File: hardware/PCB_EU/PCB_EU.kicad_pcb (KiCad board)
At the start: 4 copper layers, 100 x 100 mm, 203 parts, among them J101 24 V IN, J201 UART 3V3, J301 MEM2061 SPI, J401 SHT 3V3 / GND, J402 SHT SDA / SCL, J403 FLOAT / GND, J411 FAN1: GND / +12, J412 FAN1: TACH / PWM, J421 FAN2: GND / +12, J422 FAN2: TACH / PWM, J501 LED1 + / GND, J601 LED2 + / GND, J602 BAR2 + / GND, J701 PTC + / RETURN, J702 PUMP + / RETURN, Q102 IRF1010ESPBF, Q411 FAN1 AO3422, Q421 FAN2 AO3422, Q501 TK22E10N1, Q601 TK22E10N1, Q701 BC847B-DIO, Q702 BC857B, Q703 IRF1010ESPBF, Q704 AO3422, SW201 RESET, SW202 BOOT, U101 L7987 3A, U102 INA226, U201 AP63203WU-7, U202 ESP32-WROOM-32E-N4, U301 MCP7940N-I/SN, U401 USBLC6-2SC6, U402 USBLC6-2SC6, U501 LM3429MH/NOPB, U601 LM3429MH/NOPB, U802 LM2903D-ST, Y301 32.768k CL7p

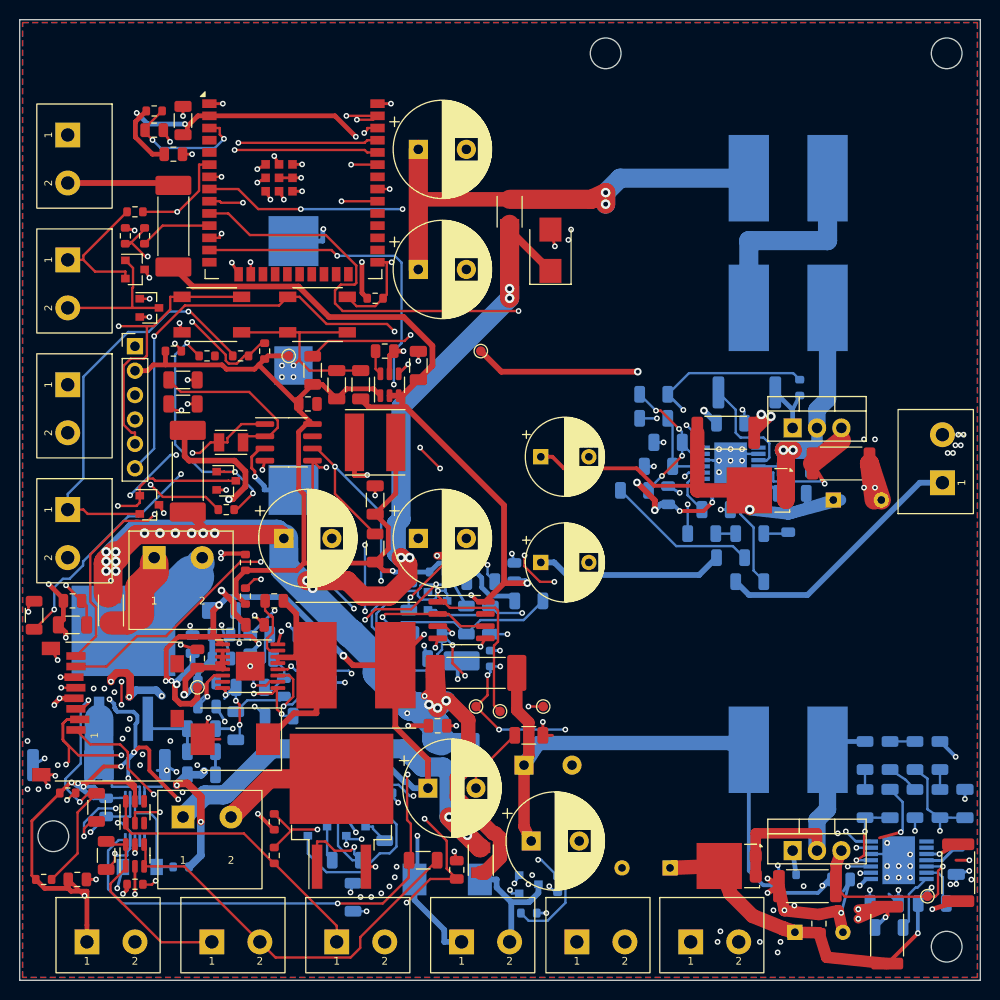
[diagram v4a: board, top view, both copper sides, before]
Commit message: PCB_EU: all terminals at the board edges, no HS2, fans on KF2510-4A, SHT4x on XH2.54-4P-90
Per Igors (22.10.2026):
- stack stated as 1 oz outer / 0.5 oz inner in DESIGN.md;
- heatsink HS2 removed from the LED2 channel (Q601 runs without a heatsink,
  about 54 C rise, to be measured on the prototype), freed area used for the
  pump terminal J702 and its parts at the right edge;
- J101, J201, J411, J421, J401, J403, J701, J702 moved so that every cable
  entry faces the board edge; J701 changed from DG301R to DG306;
- fan connectors J411/J421 are 4-pin KF2510-4A headers (Molex KK-254
  footprint), J412/J422 removed;
- SHT4x on one right-angle XH2.54-4P-90 header J401 (JST XH S4B-XH-A
  footprint), J402 removed;
- input, trunk and PTC copper re-routed in routing.json; the F101.2 trunk
  now starts with a 2.4 mm neck inside the pad (it was not attached before);
- BOM: quantities and total (82.50 EUR) unchanged, the new rows have no shop
  or price and are flagged for the BOM review.

Checks (KiCad 10.0.7): ERC 0, 56 connectivity checks, 22639 placement checks,
DRC 0 / parity 0 / unconnected 0, rebuild from the repository is byte-identical.
ampacity.py: worst IPC-2221 rise 38 C, three vias above the 2 A rule of thumb.

Co-Authored-By: Claude Sonnet 5.5 <noreply@anthropic.com>
Claude-Session: https://claude.ai/code/session_01AxccZX6Cb4FnRKJMrFYMSX
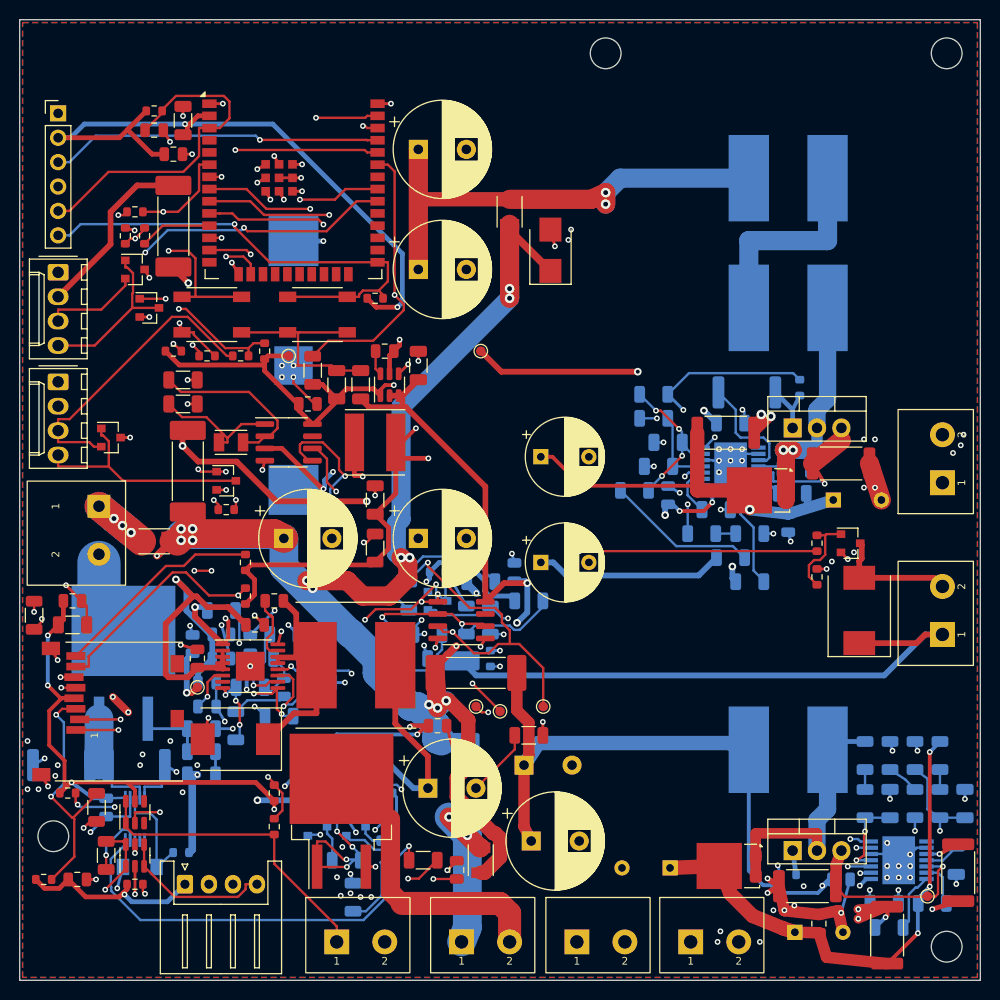
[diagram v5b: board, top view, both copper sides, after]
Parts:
- removed J402: SHT SDA / SCL, EU_Mechanical:TerminalBlock_Degson_DG306-5.0_1x02
- removed J412: FAN1: TACH / PWM, EU_Mechanical:TerminalBlock_Degson_DG306-5.0_1x02
- removed J422: FAN2: TACH / PWM, EU_Mechanical:TerminalBlock_Degson_DG306-5.0_1x02
- D701, Q704, R707, R708: moved to F.Cu
- J401: value SHT 3V3 / GND -> SHT4x XH2.54-4P-90; footprint EU_Mechanical:TerminalBlock_Degson_DG306-5.0_1x02 -> Connector_JST:JST_XH_S4B-XH-A_1x04_P2.50mm_Horizontal
- J411: value FAN1: GND / +12 -> FAN1 2510-4P; footprint EU_Mechanical:TerminalBlock_Degson_DG306-5.0_1x02 -> Connector_Molex:Molex_KK-254_AE-6410-04A_1x04_P2.54mm_Vertical
- J421: value FAN2: GND / +12 -> FAN2 2510-4P; footprint EU_Mechanical:TerminalBlock_Degson_DG306-5.0_1x02 -> Connector_Molex:Molex_KK-254_AE-6410-04A_1x04_P2.54mm_Vertical
- J701: footprint EU_Mechanical:TerminalBlock_Degson_DG301R-5.0_1x02 -> EU_Mechanical:TerminalBlock_Degson_DG306-5.0_1x02
- moved J702 59.4 mm to (96.1, 64.0), turned to 90 degrees
- moved D701 51.2 mm to (87.4, 61.5), turned to 90 degrees
- moved Q704 48.8 mm to (86.5, 54.5)
- moved R708 46.1 mm to (83.0, 58.0), turned to 90 degrees
- moved R707 44.6 mm to (83.0, 54.5)
- moved J701 31.8 mm to (46.0, 96.0)
- moved J201 25.5 mm to (4.00, 9.75)
- moved J411 14.3 mm to (4.00, 26.3)
- moved J401 11.8 mm to (17.2, 90.0)
- moved F101 8.49 mm to (14.0, 54.3), turned to 0 degrees
- moved D421 8.06 mm to (9.50, 43.5)
- moved J101 7.85 mm to (8.25, 50.6), turned to -90 degrees
- moved R403 3.00 mm to (26.5, 84.0)
- moved R404 3.00 mm to (26.5, 80.5)
- moved R113 1.50 mm to (16.8, 86.7)
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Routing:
- net +24V_FUSED: track 249.4 -> 196.6 mm, vias 33 -> 19
- net SD_MOSI_GPIO: track 135.2 -> 94.0 mm, vias 8 -> 2
- net PUMP_GPIO: track 115.6 -> 83.6 mm, vias 4 -> 2
- net +3V3: track 357.5 -> 326.5 mm, vias 22 -> 15
- net +24V_PUMP: track 34.5 -> 61.5 mm, vias 2 -> 0
- net FLOAT_GPIO: track 120.9 -> 94.7 mm, vias 7 -> 3
- net +24V_PTC: track 43.6 -> 18.5 mm
- net BLOCK_OC: track 64.2 -> 48.2 mm, vias 5 -> 9
- net LED1_LED_POS: track 58.8 -> 43.5 mm, vias 2 -> 3
- net LED_PWM_GPIO: track 80.0 -> 64.7 mm
- net SD_DAT1: track 36.6 -> 22.0 mm, vias 3 -> 0
- net I2C_SDA: track 141.4 -> 127.8 mm, vias 7 -> 4
- net UART_RX: track 48.4 -> 34.9 mm
- net PTC_GPIO: track 90.3 -> 78.9 mm, vias 5 -> 2
- net FAN2_TACH_EXT: track 42.6 -> 31.4 mm, vias 1 -> 0
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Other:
- board text removed: "HS2 RESERVE ONLY"
